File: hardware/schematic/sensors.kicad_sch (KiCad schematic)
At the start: 51 parts, among them J4 PZ254V-11-02P, J5 2.54-4P, J6 2.54-4P, J7 2.54-4P, J8 2.54-4P, SW1 TSA016A2518A, SW2 TSA016A2518A, U3 INA350ABSIDDFR, U4 W25Q16JVUXIQ, U5 TPS76925DBVR, U6 TLV333, U7 RP2040, X1 X322512MSB4SI

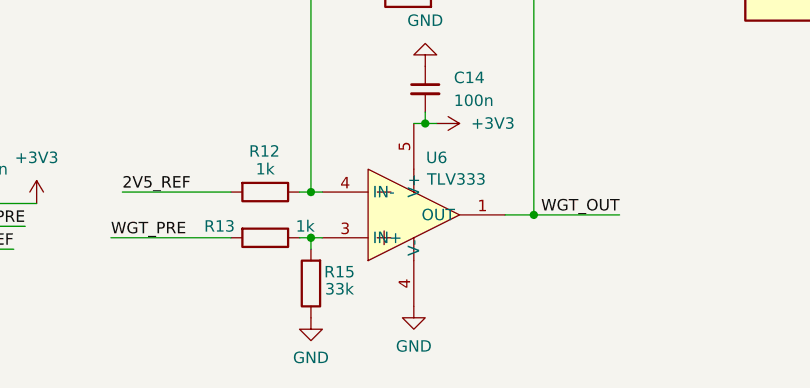
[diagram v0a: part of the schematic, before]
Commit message: fix: correct symbol for op amp
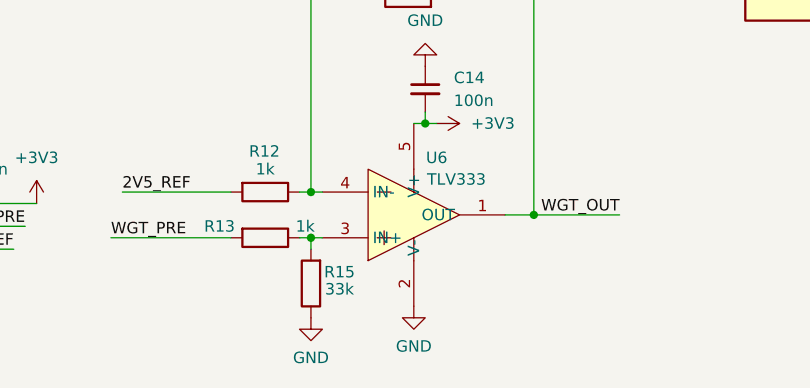
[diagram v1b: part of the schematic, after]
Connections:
- net GND: now also U6.2 (V-); no longer U6.4 (V-)
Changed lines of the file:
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@@
 		(pin "1"
 		)
-		(pin "4"
+		(pin "2"
 		)
 		(pin "4"

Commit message: feat: upload rev 3.1 schematic
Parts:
- J4, TP19, TP20, TP21, TP22, TP23, TP24, TP25, TP26, TP27: now in the parts list
- J5, J6, J7, J8: value 2.54-4P -> XY308-2.54-4P; LCSC Part (none) -> C915913
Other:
- note removed: "ADC"
- moved on the sheet: C11, C12, C13, C14, C15, C25, C26, C27, D5, J5, J6, J7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
